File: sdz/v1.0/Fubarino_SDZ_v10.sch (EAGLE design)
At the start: 39 parts, among them IC1 PIC32MZXXXXECX064TQFP-10X10, IC2 MCP1702T-3302E/MB, IC3 DSC1033_MICREL_OSCILLATOR3.2X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, J1 MICRO_SD_CARD_SOCKET, J2 M28USEPIN1, J3 M28NOPIN1, J4 MICRO-USB-5P-340015001, J5 MICRO-SDCARD-CONNECTOR-330006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, Q2 32.768 KHz

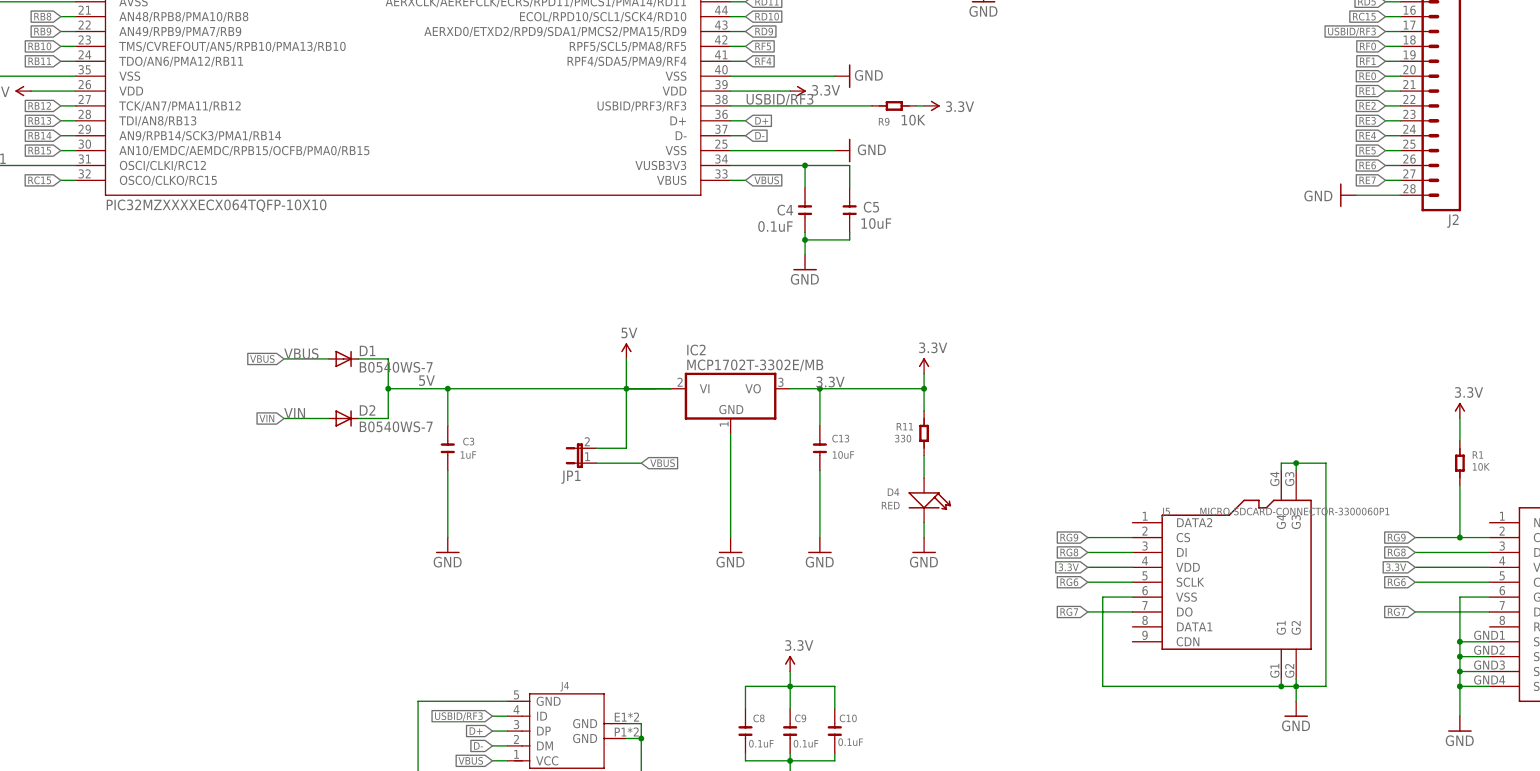
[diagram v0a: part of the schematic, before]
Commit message: Ooooops. Bad footprint for CPU. Got boards back and they had solder mask on all pins. Updated to new footprint, found D-/D+ swap bug, and send out for new boards.
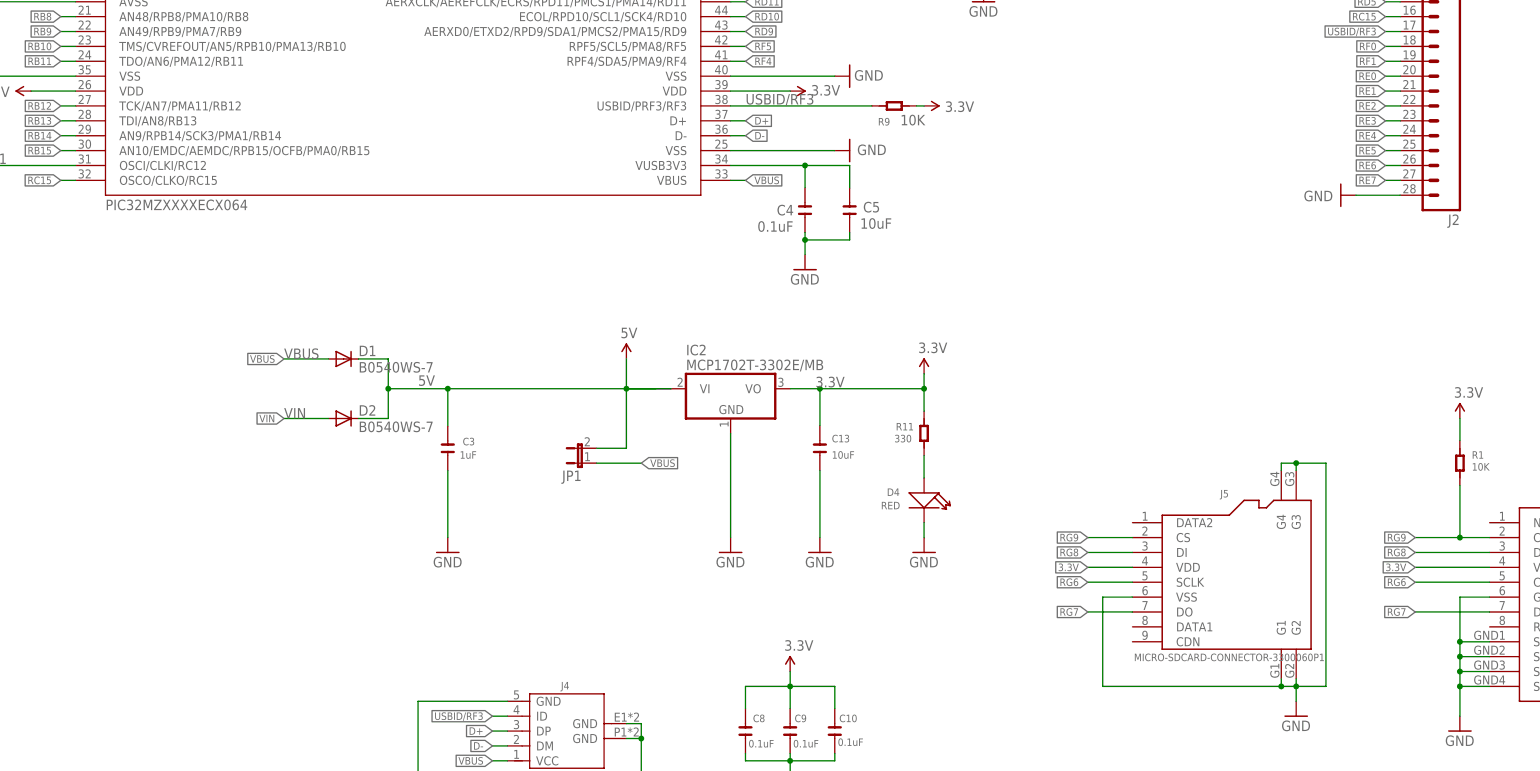
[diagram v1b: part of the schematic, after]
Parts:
- IC1: value PIC32MZXXXXECX064TQFP-10X10 -> PIC32MZXXXXECX064; device SchmalzHaus:PIC32MZXXXXECX064TQFP-10X10 -> SchmalzHaus:PIC32MZXXXXECX064
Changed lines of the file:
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@@
 <?xml version="1.0" encoding="utf-8"?>
 <!DOCTYPE eagle SYSTEM "eagle.dtd">
-<eagle version="6.4">
+<eagle version="6.5.0">
 <drawing>
 <settings>
@@
 <grid distance="0.1" unitdist="inch" unit="inch" style="lines" multiple="1" display="no" altdistance="0.01" altunitdist="inch" altunit="inch"/>
 <layers>
-<layer number="1" name="Top" color="4" fill="1" visible="no" active="no"/>
-<layer number="2" name="Route2" color="1" fill="3" visible="no" active="no"/>
-<layer number="3" name="Route3" color="4" fill="3" visible="no" active="no"/>
-<layer number="4" name="Route4" color="1" fill="4" visible="no" active="no"/>
-<layer number="5" name="Route5" color="4" fill="4" visible="no" active="no"/>
-<layer number="6" name="Route6" color="1" fill="8" visible="no" active="no"/>
-<layer number="7" name="Route7" color="4" fill="8" visible="no" active="no"/>
-<layer number="8" name="Route8" color="1" fill="2" visible="no" active="no"/>
-<layer number="9" name="Route9" color="4" fill="2" visible="no" active="no"/>
-<layer number="10" name="Route10" color="1" fill="7" visible="no" active="no"/>
-<layer number="11" name="Route11" color="4" fill="7" visible="no" active="no"/>
-<layer number="12" name="Route12" color="1" fill="5" visible="no" active="no"/>
-<layer number="13" name="Route13" color="4" fill="5" visible="no" active="no"/>
-<layer number="14" name="Route14" color="1" fill="6" visible="no" active="no"/>
-<layer number="15" name="Route15" color="4" fill="6" visible="no" active="no"/>
-<layer number="16" name="Bottom" color="1" fill="1" visible="no" active="no"/>
-<layer number="17" name="Pads" color="2" fill="1" visible="no" active="no"/>
-<layer number="18" name="Vias" color="2" fill="1" visible="no" active="no"/>
-<layer number="19" name="Unrouted" color="14" fill="1" visible="no" active="no"/>
-<layer number="20" name="Dimension" color="15" fill="1" visible="no" active="no"/>
-<layer number="21" name="tPlace" color="16" fill="1" visible="no" active="no"/>
-<layer number="22" name="bPlace" color="14" fill="1" visible="no" active="no"/>
-<layer number="23" name="tOrigins" color="15" fill="1" visible="no" active="no"/>
-<layer number="24" name="bOrigins" color="15" fill="1" visible="no" active="no"/>
-<layer number="25" name="tNames" color="7" fill="1" visible="no" active="no"/>
-<layer number="26" name="bNames" color="7" fill="1" visible="no" active="no"/>
-<layer number="27" name="tValues" color="7" fill="1" visible="no" active="no"/>
-<layer number="28" name="bValues" color="7" fill="1" visible="no" active="no"/>
+<layer number="1" name="Top" color="4" fill="1" visible="yes" active="no"/>
+<layer number="2" name="Route2" color="1" fill="3" visible="yes" active="no"/>
+<layer number="3" name="Route3" color="4" fill="3" visible="yes" active="no"/>
+<layer number="4" name="Route4" color="1" fill="4" visible="yes" active="no"/>
+<layer number="5" name="Route5" color="4" fill="4" visible="yes" active="no"/>
+<layer number="6" name="Route6" color="1" fill="8" visible="yes" active="no"/>
+<layer number="7" name="Route7" color="4" fill="8" visible="yes" active="no"/>
+<layer number="8" name="Route8" color="1" fill="2" visible="yes" active="no"/>
+<layer number="9" name="Route9" color="4" fill="2" visible="yes" active="no"/>
+<layer number="10" name="Route10" color="1" fill="7" visible="yes" active="no"/>
+<layer number="11" name="Route11" color="4" fill="7" visible="yes" active="no"/>
+<layer number="12" name="Route12" color="1" fill="5" visible="yes" active="no"/>
+<layer number="13" name="Route13" color="4" fill="5" visible="yes" active="no"/>
+<layer number="14" name="Route14" color="1" fill="6" visible="yes" active="no"/>
+<layer number="15" name="Route15" color="4" fill="6" visible="yes" active="no"/>
+<layer number="16" name="Bottom" color="1" fill="1" visible="yes" active="no"/>
+<layer number="17" name="Pads" color="2" fill="1" visible="yes" active="no"/>
+<layer number="18" name="Vias" color="2" fill="1" visible="yes" active="no"/>
+<layer number="19" name="Unrouted" color="14" fill="1" visible="yes" active="no"/>
+<layer number="20" name="Dimension" color="15" fill="1" visible="yes" active="no"/>
+<layer number="21" name="tPlace" color="16" fill="1" visible="yes" active="no"/>
+<layer number="22" name="bPlace" color="9" fill="1" visible="yes" active="no"/>
+<layer number="23" name="tOrigins" color="15" fill="1" visible="yes" active="no"/>
+<layer number="24" name="bOrigins" color="15" fill="1" visible="yes" active="no"/>
+<layer number="25" name="tNames" color="7" fill="1" visible="yes" active="no"/>
+<layer number="26" name="bNames" color="7" fill="1" visible="yes" active="no"/>
+<layer number="27" name="tValues" color="7" fill="1" visible="yes" active="no"/>
+<layer number="28" name="bValues" color="7" fill="1" visible="yes" active="no"/>
 <layer number="29" name="tStop" color="7" fill="3" visible="no" active="no"/>
 <layer number="30" name="bStop" color="7" fill="6" visible="no" active="no"/>
@@
 <layer number="35" name="tGlue" color="7" fill="4" visible="no" active="no"/>
 <layer number="36" name="bGlue" color="7" fill="5" visible="no" active="no"/>
-<layer number="37" name="tTest" color="7" fill="1" visible="no" active="no"/>
-<layer number="38" name="bTest" color="7" fill="1" visible="no" active="no"/>
+<layer number="37" name="tTest" color="7" fill="1" visible="yes" active="no"/>
+<layer number="38" name="bTest" color="7" fill="1" visible="yes" active="no"/>
 <layer number="39" name="tKeepout" color="4" fill="11" visible="no" active="no"/>
 <layer number="40" name="bKeepout" color="1" fill="11" visible="no" active="no"/>
@@
 <layer number="44" name="Drills" color="7" fill="1" visible="no" active="no"/>
 <layer number="45" name="Holes" color="7" fill="1" visible="no" active="no"/>
-<layer number="46" name="Milling" color="3" fill="1" visible="no" active="no"/>
-<layer number="47" name="Measures" color="7" fill="1" visible="no" active="no"/>
-<layer number="48" name="Document" color="7" fill="1" visible="no" active="no"/>
-<layer number="49" name="Reference" color="7" fill="1" visible="no" active="no"/>
-<layer number="50" name="dxf" color="7" fill="1" visible="no" active="no"/>
-<layer number="51" name="tDocu" color="6" fill="1" visible="no" active="no"/>
-<layer number="52" name="bDocu" color="7" fill="1" visible="no" active="no"/>
-<layer number="53" name="tGND_GNDA" color="7" fill="9" visible="no" active="no"/>
-<layer number="54" name="bGND_GNDA" color="1" fill="9" visible="no" active="no"/>
-<layer number="56" name="wert" color="7" fill="1" visible="no" active="no"/>
+<layer number="46" name="Milling" color="3" fill="1" visible="yes" active="no"/>
+<layer number="47" name="Measures" color="7" fill="1" visible="yes" active="no"/>
+<layer number="48" name="Document" color="7" fill="1" visible="yes" active="no"/>
+<layer number="49" name="Reference" color="7" fill="1" visible="yes" active="no"/>
+<layer number="50" name="dxf" color="7" fill="1" visible="yes" active="no"/>
+<layer number="51" name="tDocu" color="6" fill="1" visible="yes" active="no"/>
+<layer number="52" name="bDocu" color="7" fill="1" visible="yes" active="no"/>
+<layer number="53" name="tGND_GNDA" color="7" fill="9" visible="yes" active="no"/>
+<layer number="54" name="bGND_GNDA" color="1" fill="9" visible="yes" active="no"/>
+<layer number="56" name="wert" color="7" fill="1" visible="yes" active="no"/>
 <layer number="91" name="Nets" color="2" fill="1" visible="yes" active="yes"/>
 <layer number="92" name="Busses" color="1" fill="1" visible="yes" active="yes"/>
@@
 <part name="U$4" library="SchmalzHausPublic" deviceset="CHIPKIT" device="2MM"/>
 <part name="U$5" library="SchmalzHausPublic" deviceset="CHIPKIT" device="2MM"/>
-<part name="IC1" library="SchmalzHaus" deviceset="PIC32MZXXXXECX064" device="TQFP-10X10"/>
+<part name="IC1" library="SchmalzHaus" deviceset="PIC32MZXXXXECX064" device=""/>
 <part name="GND15" library="SparkFun02-20-08" deviceset="GND" device=""/>
 <part name="P+13" library="SparkFun02-20-08" deviceset="3.3V" device=""/>
@@
 VOUT and connect
 JP1 for USB host</text>
+<wire x1="195.58" y1="147.32" x2="195.58" y2="132.08" width="0.1524" layer="98" style="longdash"/>
+<wire x1="195.58" y1="132.08" x2="223.52" y2="132.08" width="0.1524" layer="98" style="longdash"/>
+<wire x1="223.52" y1="132.08" x2="223.52" y2="147.32" width="0.1524" layer="98" style="longdash"/>
+<wire x1="223.52" y1="147.32" x2="195.58" y2="147.32" width="0.1524" layer="98" style="longdash"/>
+<text x="197.612" y="133.858" size="1.778" layer="98">Do Not Populate</text>
 </plain>
 <instances>
@@
 <attribute name="VALUE" x="354.076" y="60.706" size="1.27" layer="96" font="vector" ratio="10"/>
 </instance>
-<instance part="J5" gate="J" x="264.16" y="78.74"/>
+<instance part="J5" gate="J" x="264.16" y="78.74" smashed="yes">
+<attribute name="NAME" x="261.366" y="93.218" size="1.27" layer="95" ratio="10"/>
+<attribute name="VALUE" x="246.634" y="65.278" size="1.27" layer="96" ratio="10"/>
+</instance>
 <instance part="GND26" gate="1" x="274.32" y="55.88"/>
 </instances>
